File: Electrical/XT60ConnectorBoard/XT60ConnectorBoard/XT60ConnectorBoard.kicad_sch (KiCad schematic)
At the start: 13 parts, among them J1 XT60PW-M, J10 XT60PW-M, J11 XT60PW-M, J12 XT60PW-M, J13 XT60PW-M, J2 XT60PW-M, J3 XT60PW-M, J4 XT60PW-M, J5 XT60PW-M, J6 XT60PW-M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

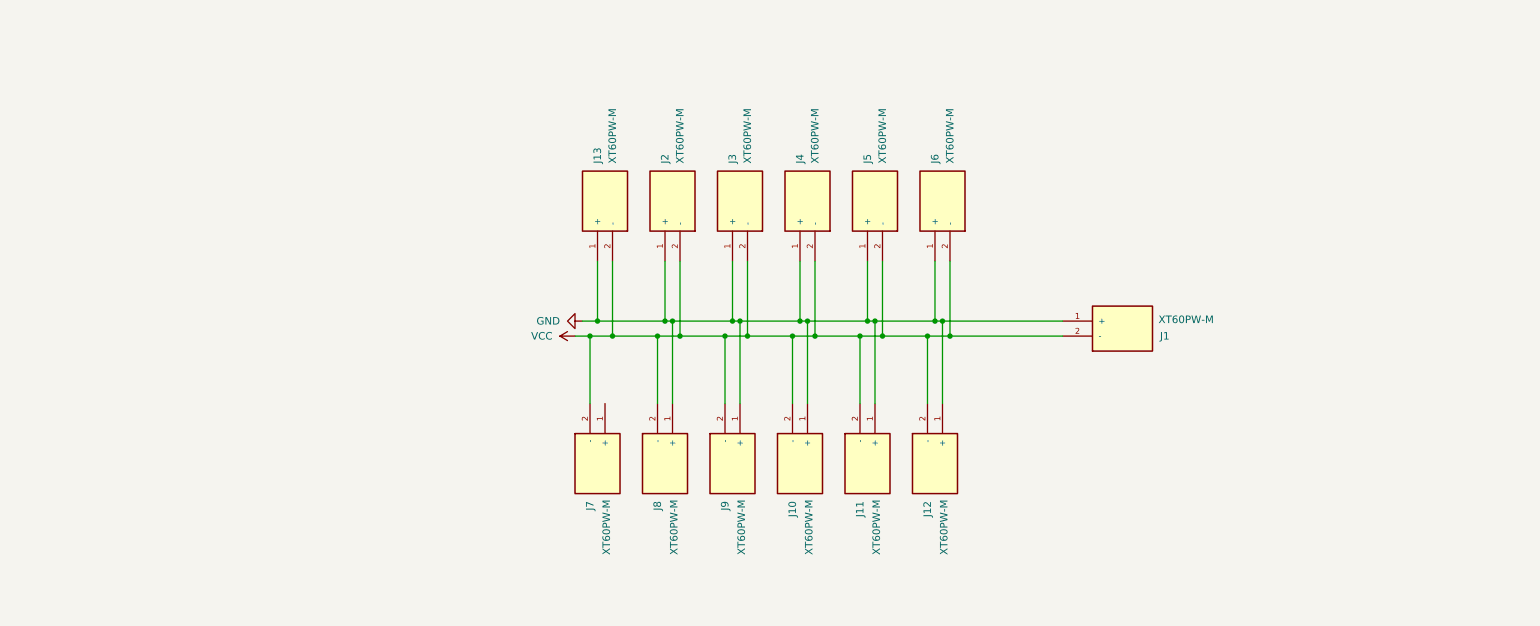
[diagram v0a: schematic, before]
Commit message: XT60 Board
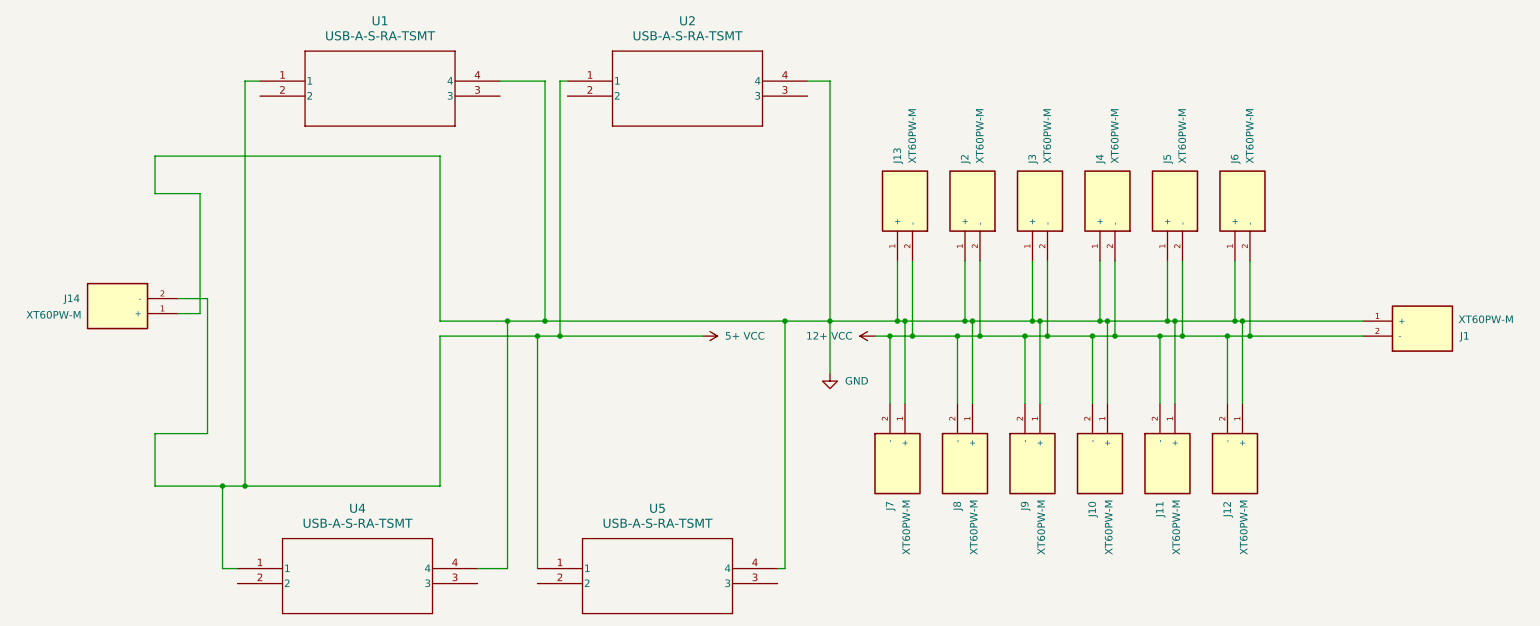
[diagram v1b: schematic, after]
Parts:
- added J14: XT60PW-M, Connector_AMASS:AMASS_XT60PW-M_1x02_P7.20mm_Horizontal, symbol XT60PW-M:XT60PW-M
- added U1, U2, U4, U5: USB-A-S-RA-TSMT, USB-A-S-RA-TSMT_ADM, symbol 2025-02-23_03-18-15:USB-A-S-RA-TSMT
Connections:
- net GND: now also J7.1 (+), J14.1 (+), U1.4, U2.4, U4.4, U5.4
- net VCC renamed 12+ VCC
- new net 5+ VCC: J14.2 (-), U1.1, U2.1, U4.1, U5.1
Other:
- moved on the sheet: J1, J10, J11, J12, J13, J2, J3, J4, J5, J6, J7, J8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

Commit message: finished xt60 board
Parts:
- added J15, J16: XT60PW-M, Connector_AMASS:AMASS_XT60PW-M_1x02_P7.20mm_Horizontal, symbol XT60PW-M:XT60PW-M
- added U3, U6: USB-A-S-RA-TSMT, USB-A-S-RA-TSMT_ADM, symbol 2025-02-23_03-18-15:USB-A-S-RA-TSMT
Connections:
- net 12+ VCC: now also J15.2 (-), J16.2 (-)
- net 5+ VCC: now also U3.1, U6.1
- net GND: now also J15.1 (+), J16.1 (+), U3.4, U6.4

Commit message: xt60board
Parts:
- removed J13, J2, J3, J7, J8, J9: XT60PW-M, Connector_AMASS:AMASS_XT60PW-M_1x02_P7.20mm_Horizontal, symbol XT60PW-M:XT60PW-M
- removed U1, U2, U3, U4, U5, U6: USB-A-S-RA-TSMT, USB-A-S-RA-TSMT_ADM, symbol 2025-02-23_03-18-15:USB-A-S-RA-TSMT
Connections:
- net 5+ VCC is gone; now on net 12+ VCC: J14.2 (-)
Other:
- moved on the sheet: J1, J10, J11, J12, J14, J15, J16, J4, J5, J6
